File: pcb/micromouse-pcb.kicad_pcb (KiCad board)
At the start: 4 copper layers, 120 x 80 mm, 50 parts, among them J1 Conn_01x08, J1_MotorEncoder1 Conn_01x06, J2_MotorEncoder1 Conn_01x06, J3 Conn_01x08, J4 Conn_01x08, Q1 BS170, Q2 TEFT4300, Q3 BS170, Q4 TEFT4300, Q5 BS170, Q6 TEFT4300, Q7 BS170, Q8 TEFT4300, SW1 SW_SPDT, U0 Teensy 4.1, U2 L7805

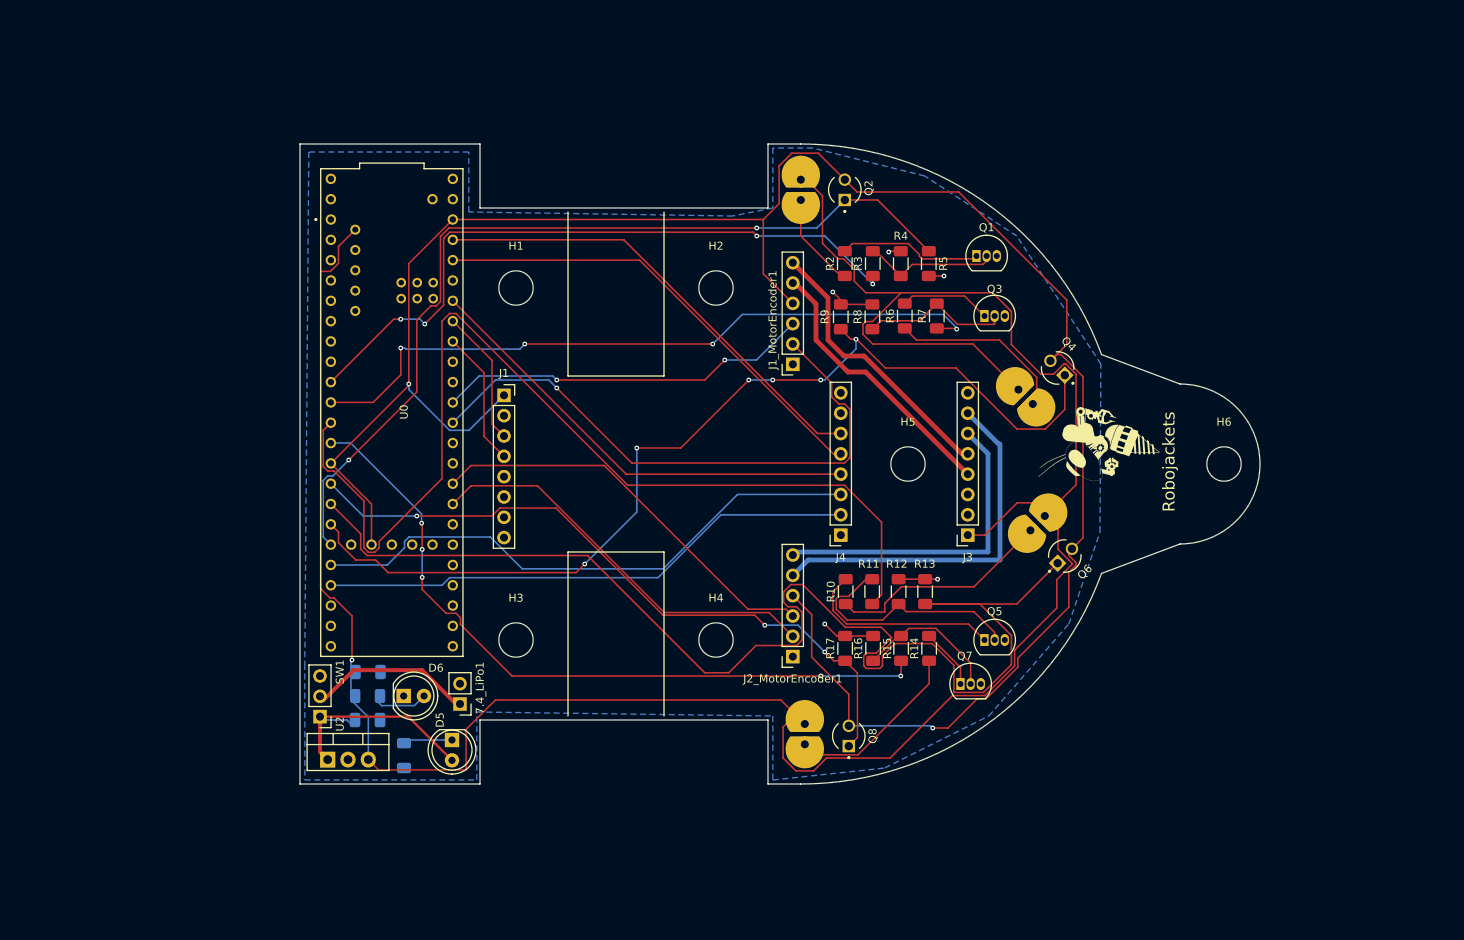
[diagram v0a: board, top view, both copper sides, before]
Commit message: Reformatted schematic; Fixed Teensy & IR footprints; Changed Board Setups
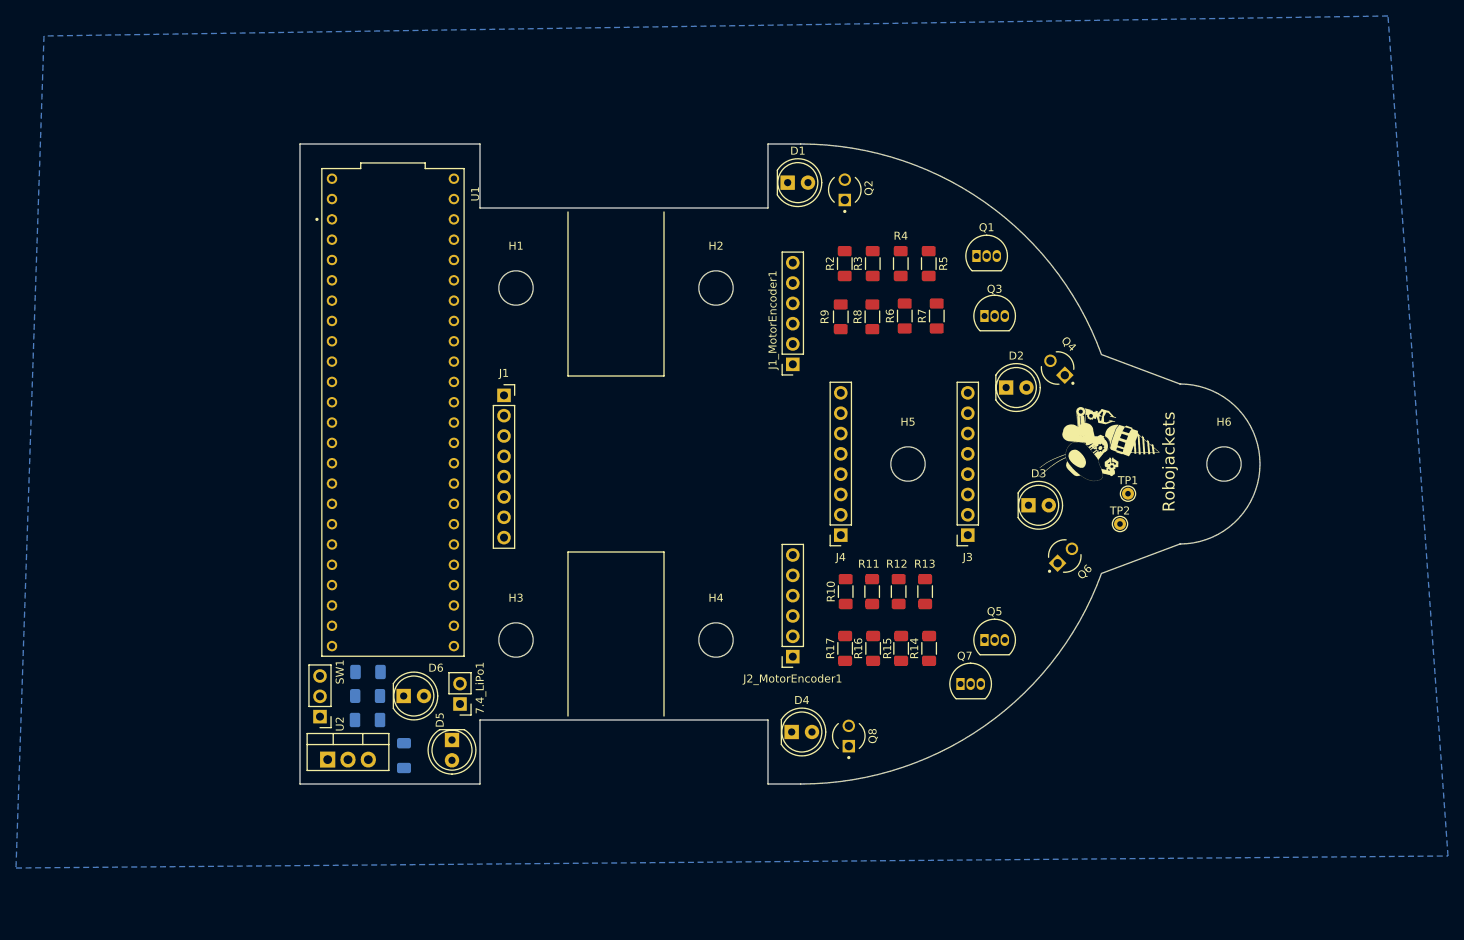
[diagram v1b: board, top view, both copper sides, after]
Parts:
- removed U0: Teensy 4.1, DEV-16771:MODULE_DEV-16771
- added TP1: TestPoint, TestPoint:TestPoint_THTPad_D1.5mm_Drill0.7mm, F.Cu at (118.5, 58.7)
- added TP2: TestPoint, TestPoint:TestPoint_THTPad_D1.5mm_Drill0.7mm, F.Cu at (117.5, 62.5)
- added U1: Teensy_4.1, micromouse:Teensy4.1_LessHoles, F.Cu at (26.6, 48.5)
- D1, D2, D3, D4: footprint SFH_4545:DIO_SFH_4545 -> micromouse:LED_D5.0mm_IR
- moved D2 2.70 mm to (103.3, 45.4), turned to 0 degrees
- moved D3 2.51 mm to (106.1, 60.2), turned to 0 degrees
- moved D1 1.87 mm to (76.0, 19.8), turned to 0 degrees
- moved D4 1.66 mm to (76.5, 88.5), turned to 0 degrees
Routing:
- net 5V: track 316.5 -> 0.00 mm, vias 1 -> 0
- net 3.3V: track 266.1 -> 0.00 mm, vias 2 -> 0
- net Receiver 3: track 161.7 -> 0.00 mm
- net Emitter 3: track 129.4 -> 0.00 mm
- net Receiver 2: track 124.9 -> 0.00 mm, vias 6 -> 0
- net Receiver 1: track 111.3 -> 0.00 mm, vias 2 -> 0
- net Emitter 4: track 91.2 -> 0.00 mm, vias 5 -> 0
- net Emitter 2: track 88.2 -> 0.00 mm, vias 4 -> 0
- net Receiver 4: track 86.2 -> 0.00 mm, vias 3 -> 0
- net Emitter 1: track 84.6 -> 0.00 mm, vias 4 -> 0
- net Signal M1_A: track 74.0 -> 0.00 mm, vias 1 -> 0
- net PWM M1_A: track 71.1 -> 0.00 mm
- net PWM M1_B: track 67.4 -> 0.00 mm
- net PWM M2_B: track 58.5 -> 0.00 mm
- net PWM M2_A: track 58.5 -> 0.00 mm
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
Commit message: Done placement
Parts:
- removed the ? at (122.5, 53.6)
- removed R1_1: R_US, Resistor_SMD:R_1206_3216Metric_Pad1.30x1.75mm_HandSolder
- removed SW1: SW_SPDT, Connector_PinHeader_2.54mm:PinHeader_1x03_P2.54mm_Vertical
- added ?: , micromouse:ROBOJACKETS, F.Cu at (141.0, 79.5)
- added ?: , micromouse:ROBOBUZZ_0.8X, F.Cu at (135.5, 65.6)
- added C3: C, Capacitor_SMD:C_1206_3216Metric_Pad1.33x1.80mm_HandSolder, F.Cu at (46.5, 90.5)
- added Q9: FQP27P06, Package_TO_SOT_THT:TO-220-3_Vertical, F.Cu at (39.9, 96.5)
- added R1: R_US, Resistor_SMD:R_1206_3216Metric_Pad1.30x1.75mm_HandSolder, F.Cu at (40.0, 90.5)
- added R18: R_US, Resistor_SMD:R_1206_3216Metric_Pad1.30x1.75mm_HandSolder, F.Cu at (35.5, 108.0)
- added R19: 4.7k, Resistor_SMD:R_1206_3216Metric_Pad1.30x1.75mm_HandSolder, F.Cu at (59.0, 57.5)
- added R20: 4.7k, Resistor_SMD:R_1206_3216Metric_Pad1.30x1.75mm_HandSolder, F.Cu at (59.0, 51.5)
- added R21: 1k, Resistor_SMD:R_1206_3216Metric_Pad1.30x1.75mm_HandSolder, F.Cu at (33.0, 21.0)
- added SW2: SW_SPDT, Button_Switch_THT:SW_Slide_SPDT_Angled_CK_OS102011MA1Q, F.Cu at (30.0, 102.1)
- added TP3: TestPoint, micromouse:TestPoint_THTPad_D2.0mm_Drill1.0mm, F.Cu at (134.0, 55.0)
- added TP4: TestPoint, micromouse:TestPoint_THTPad_D2.0mm_Drill1.0mm, F.Cu at (134.0, 58.5)
- added TP5: TestPoint, micromouse:TestPoint_THTPad_D2.0mm_Drill1.0mm, F.Cu at (103.5, 77.0)
- added TP6: TestPoint, micromouse:TestPoint_THTPad_D2.0mm_Drill1.0mm, F.Cu at (100.5, 77.0)
- 7.4_LiPo1: footprint Connector_PinHeader_2.54mm:PinHeader_1x02_P2.54mm_Vertical -> Connector_JST:JST_PH_B2B-PH-K_1x02_P2.00mm_Vertical
- C1, C2, R1_2: moved to F.Cu
- D1, D2, D3, D4: footprint micromouse:LED_D5.0mm_IR -> micromouse:DIO_SFH_4545_copy
- D5, D6: footprint LED_THT:LED_D5.0mm -> LED_SMD:LED_1206_3216Metric_Pad1.42x1.75mm_HandSolder
- R2: value R_US -> 100/75
- R3: value R_US -> 1.3k
- R4: value R_US -> 2k
- TP1, TP2: footprint TestPoint:TestPoint_THTPad_D1.5mm_Drill0.7mm -> micromouse:TestPoint_THTPad_D2.0mm_Drill1.0mm
- moved TP1 75.5 mm to (51.5, 93.5)
- moved TP2 74.5 mm to (51.5, 97.0)
- moved D5 68.7 mm to (39.0, 21.0), turned to 0 degrees
- moved C2 34.5 mm to (45.0, 108.0), turned to 90 degrees
- moved D6 33.3 mm to (51.0, 108.0), turned to 90 degrees
- moved R1_2 32.9 mm to (51.0, 102.0), turned to -90 degrees
- moved R9 32.1 mm to (114.0, 43.0), turned to -90 degrees
- moved R2 31.5 mm to (114.5, 31.9), turned to -90 degrees
- moved R16 31.2 mm to (113.5, 94.0), turned to -90 degrees
- moved R10 30.9 mm to (113.0, 79.5), turned to 180 degrees
- moved R13 29.3 mm to (118.0, 86.5)
- moved C1 26.8 mm to (40.0, 108.0), turned to -90 degrees
- moved R6 26.7 mm to (114.0, 49.5), turned to -90 degrees
- moved D3 26.0 mm to (123.0, 79.9), turned to 45 degrees
- moved D4 25.5 mm to (95.0, 106.0), turned to 90 degrees
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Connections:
- net M1_A renamed POW_M1_A
- net M1_B renamed POW_M1_B
- net M2_A renamed POW_M2_A
- net M2_B renamed POW_M2_B
- C2 pad 1: 5V -> GND
- C2 pad 2: GND -> 5V
- D5 pad 1: Net-(D5-K) -> GND
- D5 pad 2: 7.4V -> Net-(D5-A)
- J1_MotorEncoder1 pad 2: Signal M1_A -> ENC_M1_A
- J1_MotorEncoder1 pad 3: Signal M1_B -> ENC_M1_B
- J2_MotorEncoder1 pad 2: Signal M2_A -> ENC_M2_A
- J2_MotorEncoder1 pad 3: Signal M2_B -> ENC_M2_B
- J3 pad 2: unconnected-(J3-Pin_2-Pad2) -> Net-(J3-Pin_2)
- J4 pad 1: unconnected-(J4-Pin_1-Pad1) -> PWMA_6612
- J4 pad 7: unconnected-(J4-Pin_7-Pad7) -> PWMB_6612
- U1 pad 0: unconnected-(U1-RX1-Pad0) -> Net-(U1-RX1)
- U1 pad 10: Emitter 2 -> unconnected-(U1-CS1-Pad10)
- U1 pad 11: Emitter 3 -> PWMA_6612
- U1 pad 12: Emitter 4 -> PWMB_6612
- U1 pad 14: Signal M1_A -> unconnected-(U1-A0-Pad14)
- U1 pad 15: Signal M1_B -> unconnected-(U1-A1-Pad15)
- U1 pad 34: unconnected-(U1-RX8-Pad34) -> ENC_M1_A
- U1 pad 35: unconnected-(U1-TX8-Pad35) -> ENC_M1_B
- U1 pad 36: unconnected-(U1-CS2-Pad36) -> ENC_M2_A
- U1 pad 37: unconnected-(U1-CS3-Pad37) -> ENC_M2_B
- U1 pad 38: unconnected-(U1-A14-Pad38) -> Emitter 1
- U1 pad 39: unconnected-(U1-A15-Pad39) -> Emitter 2
- U1 pad 40: Signal M2_A -> Emitter 3
- U1 pad 41: Signal M2_B -> Emitter 4
- U1 pad 9: Emitter 1 -> unconnected-(U1-OUT1C-Pad9)
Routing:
- added copper zone on In1.Cu, net GND
- removed copper zone on B.Cu, net GND
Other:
- board size 120 x 80 mm -> 126.2 x 95 mm
- board text removed: "Robojackets"

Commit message: Finished Routing!
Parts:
- moved C3 6.52 mm to (40.0, 90.0), turned to 180 degrees
- moved R1 6.52 mm to (46.5, 90.0), turned to 180 degrees
- moved ? 3.64 mm to (134.5, 69.1)
- moved ? 1.41 mm to (140.0, 78.5)
- moved D1 1.27 mm to (95.0, 24.3)
- moved Q2 1.27 mm to (100.5, 24.3)
- moved TP5 0.50 mm to (103.5, 76.5)
- moved TP6 0.50 mm to (100.5, 76.5)
- moved D4 0.27 mm to (95.0, 105.7)
- moved Q8 0.27 mm to (100.5, 105.7)
- turned D5 to 180 degrees
- turned R18 to -90 degrees
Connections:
- net 5V renamed +5V
- J1 pad 1: 3.3V -> +3.3V
- J1_MotorEncoder1 pad 4: 3.3V -> +3.3V
- J2_MotorEncoder1 pad 4: 3.3V -> +3.3V
- Q2 pad C: 3.3V -> +3.3V
- Q4 pad C: 3.3V -> +3.3V
- Q6 pad C: 3.3V -> +3.3V
- Q8 pad C: 3.3V -> +3.3V
- R19 pad 1: 3.3V -> +3.3V
- R20 pad 1: 3.3V -> +3.3V
- TP3 pad 1: 3.3V -> +3.3V
- TP4 pad 1: 3.3V -> +3.3V
- U1 pad 11: PWMA_6612 -> unconnected-(U1-MOSI-Pad11)
- U1 pad 12: PWMB_6612 -> unconnected-(U1-MISO-Pad12)
- U1 pad 14: unconnected-(U1-A0-Pad14) -> PWMB_6612
- U1 pad 15: unconnected-(U1-A1-Pad15) -> PWMA_6612
- U1 pad 24: Receiver 4 -> Receiver 1
- U1 pad 25: Receiver 3 -> Emitter 1
- U1 pad 26: Receiver 2 -> Emitter 4
- U1 pad 27: Receiver 1 -> Receiver 4
- U1 pad 34: ENC_M1_A -> ENC_M2_A
- U1 pad 35: ENC_M1_B -> ENC_M2_B
- U1 pad 36: ENC_M2_A -> ENC_M1_A
- U1 pad 37: ENC_M2_B -> ENC_M1_B
- U1 pad 38: Emitter 1 -> Receiver 3
- U1 pad 39: Emitter 2 -> Emitter 3
- U1 pad 40: Emitter 3 -> Emitter 2
- U1 pad 41: Emitter 4 -> Receiver 2
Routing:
- net Receiver 2: track 0.00 -> 93.4 mm
- net Receiver 1: track 0.00 -> 91.3 mm
- net PWM M1_A: track 0.00 -> 88.4 mm
- net Receiver 3: track 0.00 -> 87.8 mm
- net PWM M1_B: track 0.00 -> 86.8 mm
- net Emitter 1: track 0.00 -> 86.1 mm
- net Receiver 4: track 0.00 -> 83.5 mm
- net PWMB_6612: track 0.00 -> 81.1 mm, vias 0 -> 2
- net Emitter 4: track 0.00 -> 77.5 mm
- net PWM M2_B: track 0.00 -> 73.7 mm
- net PWM M2_A: track 0.00 -> 72.2 mm
- net PWMA_6612: track 0.00 -> 66.7 mm, vias 0 -> 2
- net STBY: track 0.00 -> 65.5 mm
- net Emitter 2: track 0.00 -> 63.6 mm
- net Emitter 3: track 0.00 -> 63.3 mm
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- added copper zone on In2.Cu, net +3.3V
- added copper zone on In2.Cu, net +5V

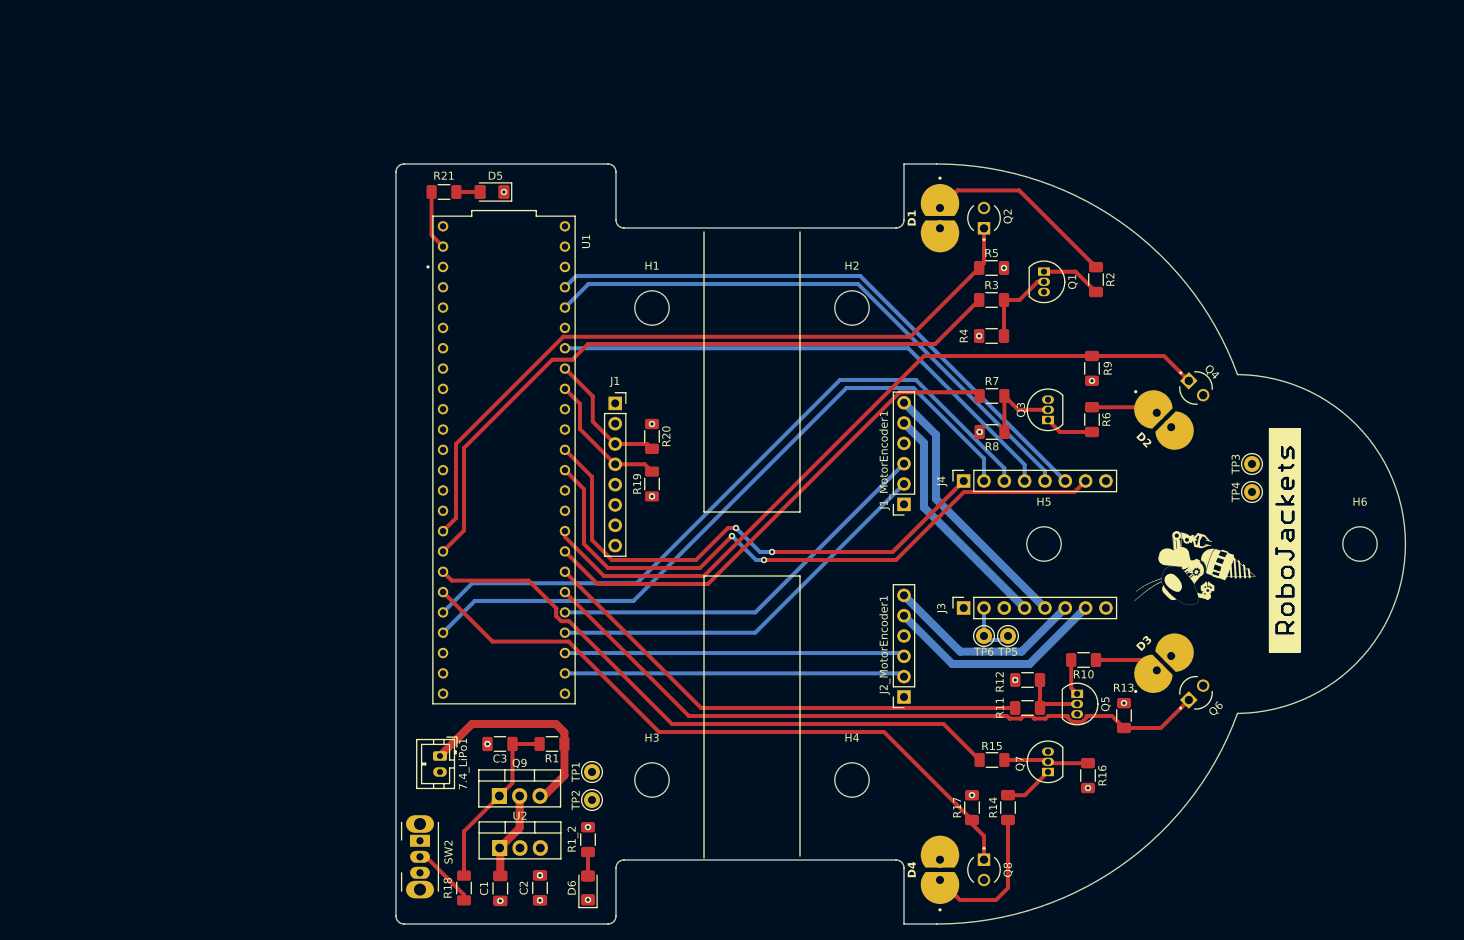
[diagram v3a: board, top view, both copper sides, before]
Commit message: Added trim pots and DNP resistors
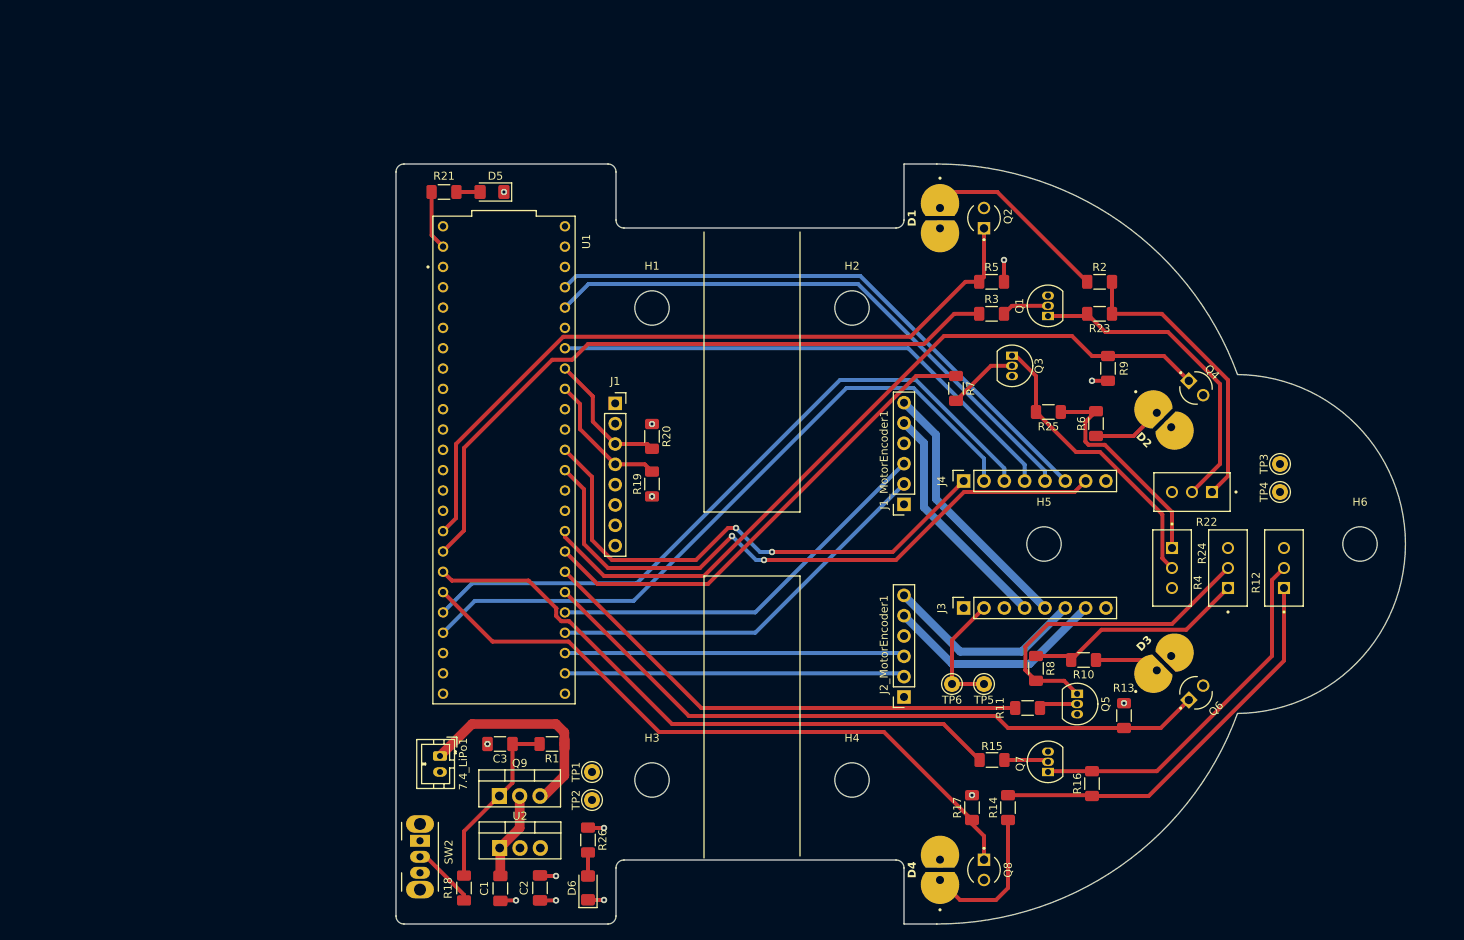
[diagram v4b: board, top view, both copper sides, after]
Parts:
- removed ?: , micromouse:ROBOBUZZ_0.8X
- removed ?: , micromouse:ROBOJACKETS
- removed R1_2: R_US, Resistor_SMD:R_1206_3216Metric_Pad1.30x1.75mm_HandSolder
- added R22: R_Variable_US, micromouse:TRIM_PV36W203C01B00, F.Cu at (126.5, 58.5)
- added R23: 0, Resistor_SMD:R_1206_3216Metric_Pad1.30x1.75mm_HandSolder, F.Cu at (115.0, 36.2)
- added R24: R_Variable_US, micromouse:TRIM_PV36W203C01B00, F.Cu at (124.0, 68.0)
- added R25: 0, Resistor_SMD:R_1206_3216Metric_Pad1.30x1.75mm_HandSolder, F.Cu at (108.5, 48.5)
- added R26: 5k, Resistor_SMD:R_1206_3216Metric_Pad1.30x1.75mm_HandSolder, F.Cu at (51.0, 102.0)
- C3: value C -> 100nF
- R1: value R_US -> 1M
- R10, R14, R6: value R_US -> 40
- R11, R15, R18, R7: value R_US -> 100
- R12: value R_US -> R_Variable_US; footprint Resistor_SMD:R_1206_3216Metric_Pad1.30x1.75mm_HandSolder -> micromouse:TRIM_PV36W203C01B00
- R13, R17, R5, R9: value R_US -> 800
- R16, R8: value R_US -> 0
- R2: value 100/75 -> 40
- R4: value 2k -> R_Variable_US; footprint Resistor_SMD:R_1206_3216Metric_Pad1.30x1.75mm_HandSolder -> micromouse:TRIM_PV36W203C01B00
- moved R4 41.4 mm to (131.0, 68.0), turned to 90 degrees
- moved R12 35.0 mm to (138.0, 68.0), turned to 90 degrees
- moved R8 30.1 mm to (107.0, 80.5), turned to -90 degrees
- moved Q3 9.21 mm to (104.0, 41.5), turned to -90 degrees
- moved TP6 7.21 mm to (96.5, 82.5)
- moved TP5 6.71 mm to (100.5, 82.5)
- moved Q1 5.56 mm to (108.5, 36.5), turned to 90 degrees
- moved R7 4.60 mm to (97.0, 45.5), turned to -90 degrees
- moved TP3 3.50 mm to (137.5, 55.0)
- moved TP4 3.50 mm to (137.5, 58.5)
- moved R9 2.00 mm to (116.0, 43.0)
- moved R3 1.73 mm to (101.5, 36.2)
- moved R5 1.73 mm to (101.5, 32.2)
- moved R16 1.12 mm to (114.0, 95.0), turned to 90 degrees
- moved R6 0.71 mm to (114.5, 50.0), turned to 90 degrees
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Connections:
- R10 pad 2: Net-(Q5-D) -> Net-(R10-Pad2)
- R12 pad 1: Net-(Q5-G) -> Net-(R12-Pad1)
- R12 pad 2: GND -> Net-(Q7-D)
- R14 pad 2: Net-(Q7-D) -> Net-(R12-Pad1)
- R16 pad 1: Net-(Q7-G) -> Net-(R12-Pad1)
- R16 pad 2: GND -> Net-(Q7-D)
- R2 pad 2: Net-(Q1-D) -> Net-(R2-Pad2)
- R4 pad 1: Net-(Q1-G) -> Net-(R10-Pad2)
- R4 pad 2: GND -> Net-(Q5-D)
- R6 pad 2: Net-(Q3-D) -> Net-(R24-Pad1)
- R8 pad 1: Net-(Q3-G) -> Net-(R10-Pad2)
- R8 pad 2: GND -> Net-(Q5-D)
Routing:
- net Net-(R12-Pad1): track 0.00 -> 50.6 mm
- net Net-(Q7-D): track 6.20 -> 45.6 mm
- net Net-(R2-Pad2): track 0.00 -> 36.3 mm
- net Net-(Q5-D): track 4.54 -> 40.3 mm
- net Net-(Q1-D): track 7.55 -> 40.2 mm
- net Net-(Q3-D): track 6.12 -> 37.2 mm
- net Net-(R10-Pad2): track 0.00 -> 27.9 mm
- net Net-(R24-Pad1): track 0.00 -> 27.8 mm
- net GND: track 0.00 -> 10.7 mm, vias 13 -> 9
- net Net-(J3-Pin_2): track 7.00 -> 15.2 mm
- net Net-(Q7-G): track 10.6 -> 5.79 mm
- net Net-(Q1-G): track 10.4 -> 5.91 mm
- net +5V: track 0.00 -> 4.07 mm
- net Net-(Q5-G): track 8.35 -> 4.85 mm
- net Emitter 2: track 63.6 -> 61.3 mm
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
